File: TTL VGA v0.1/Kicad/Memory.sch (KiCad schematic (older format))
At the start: 14 parts, among them U10 UM61512A, U11 74LS245, U12 74LS374, U13 74LS245, U14 74LS245, U6 G22V10, U7 G22V10, U8 74LS139, U9 UM61512A

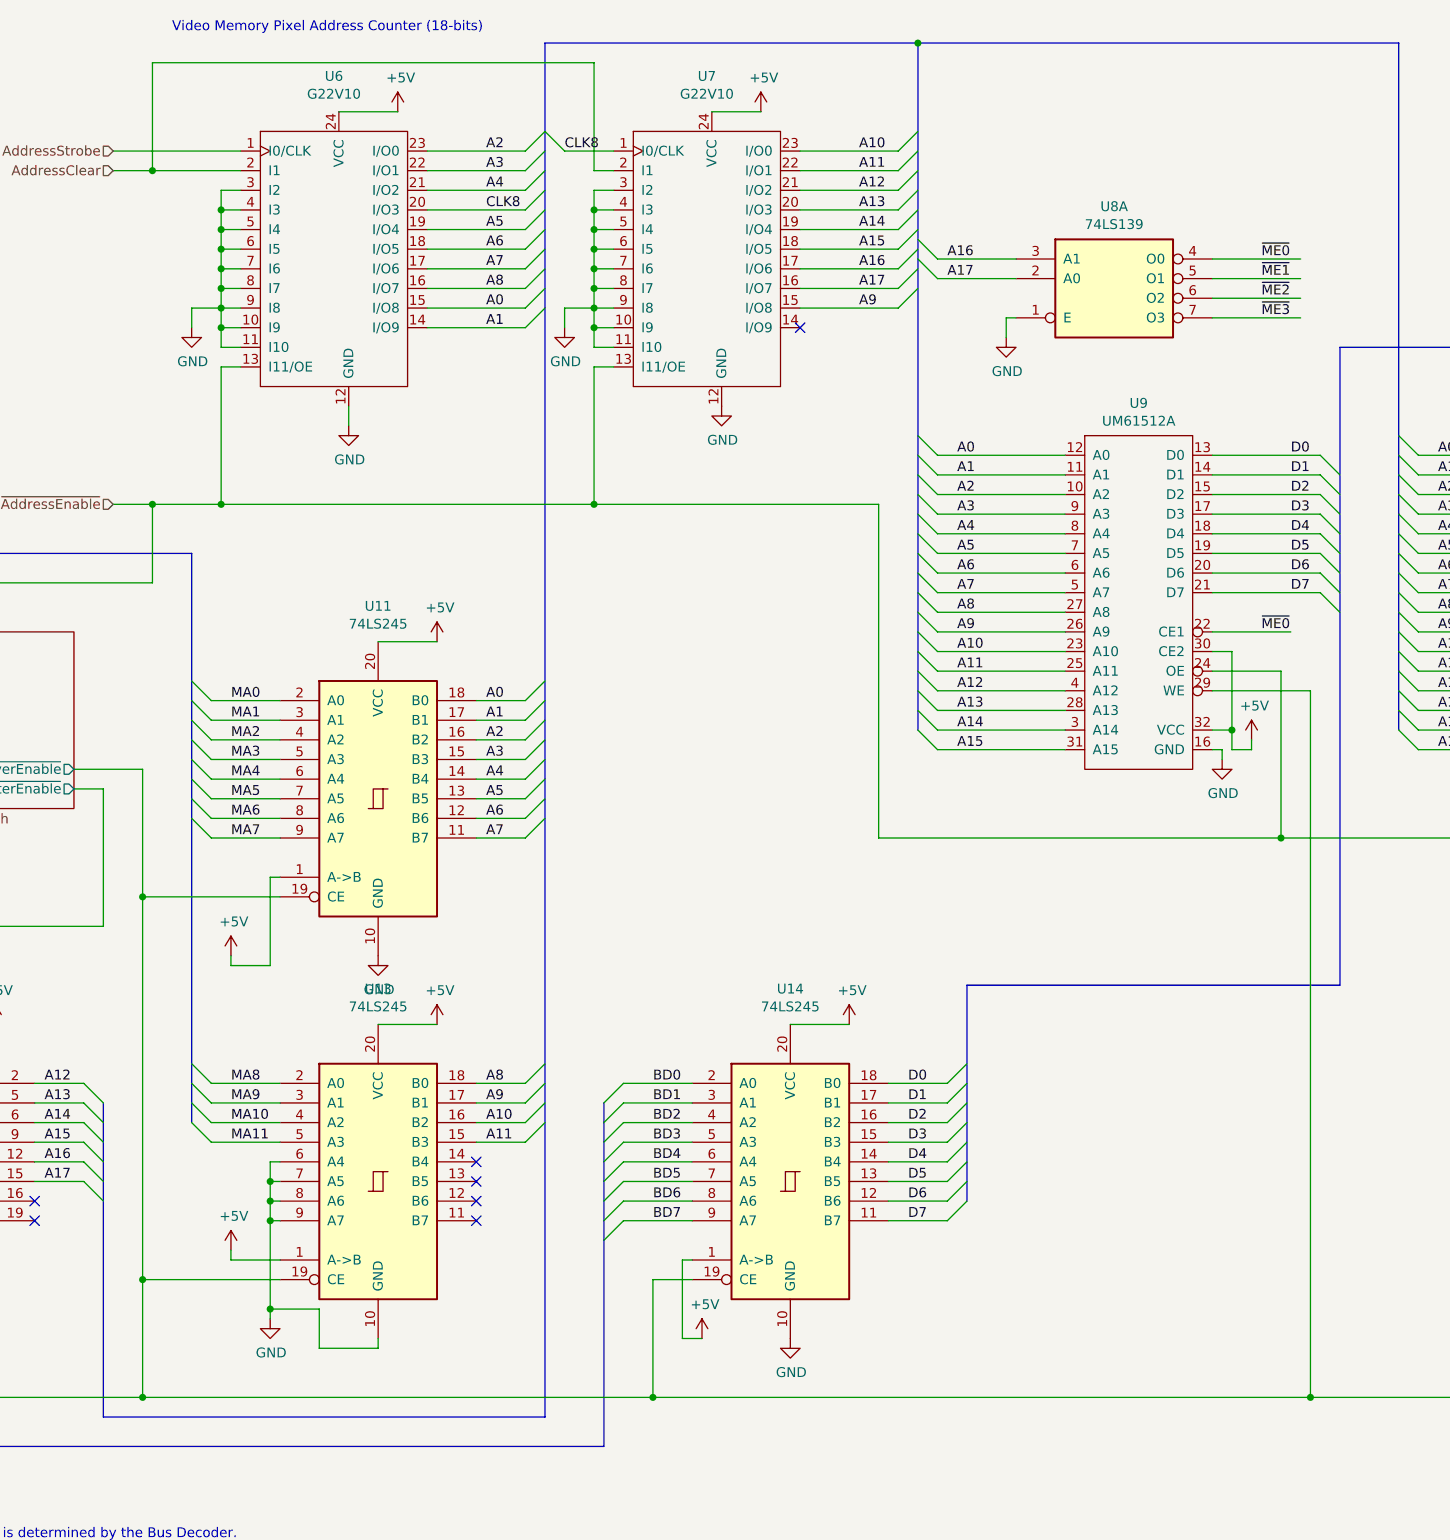
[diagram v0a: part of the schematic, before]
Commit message: vga memory interface
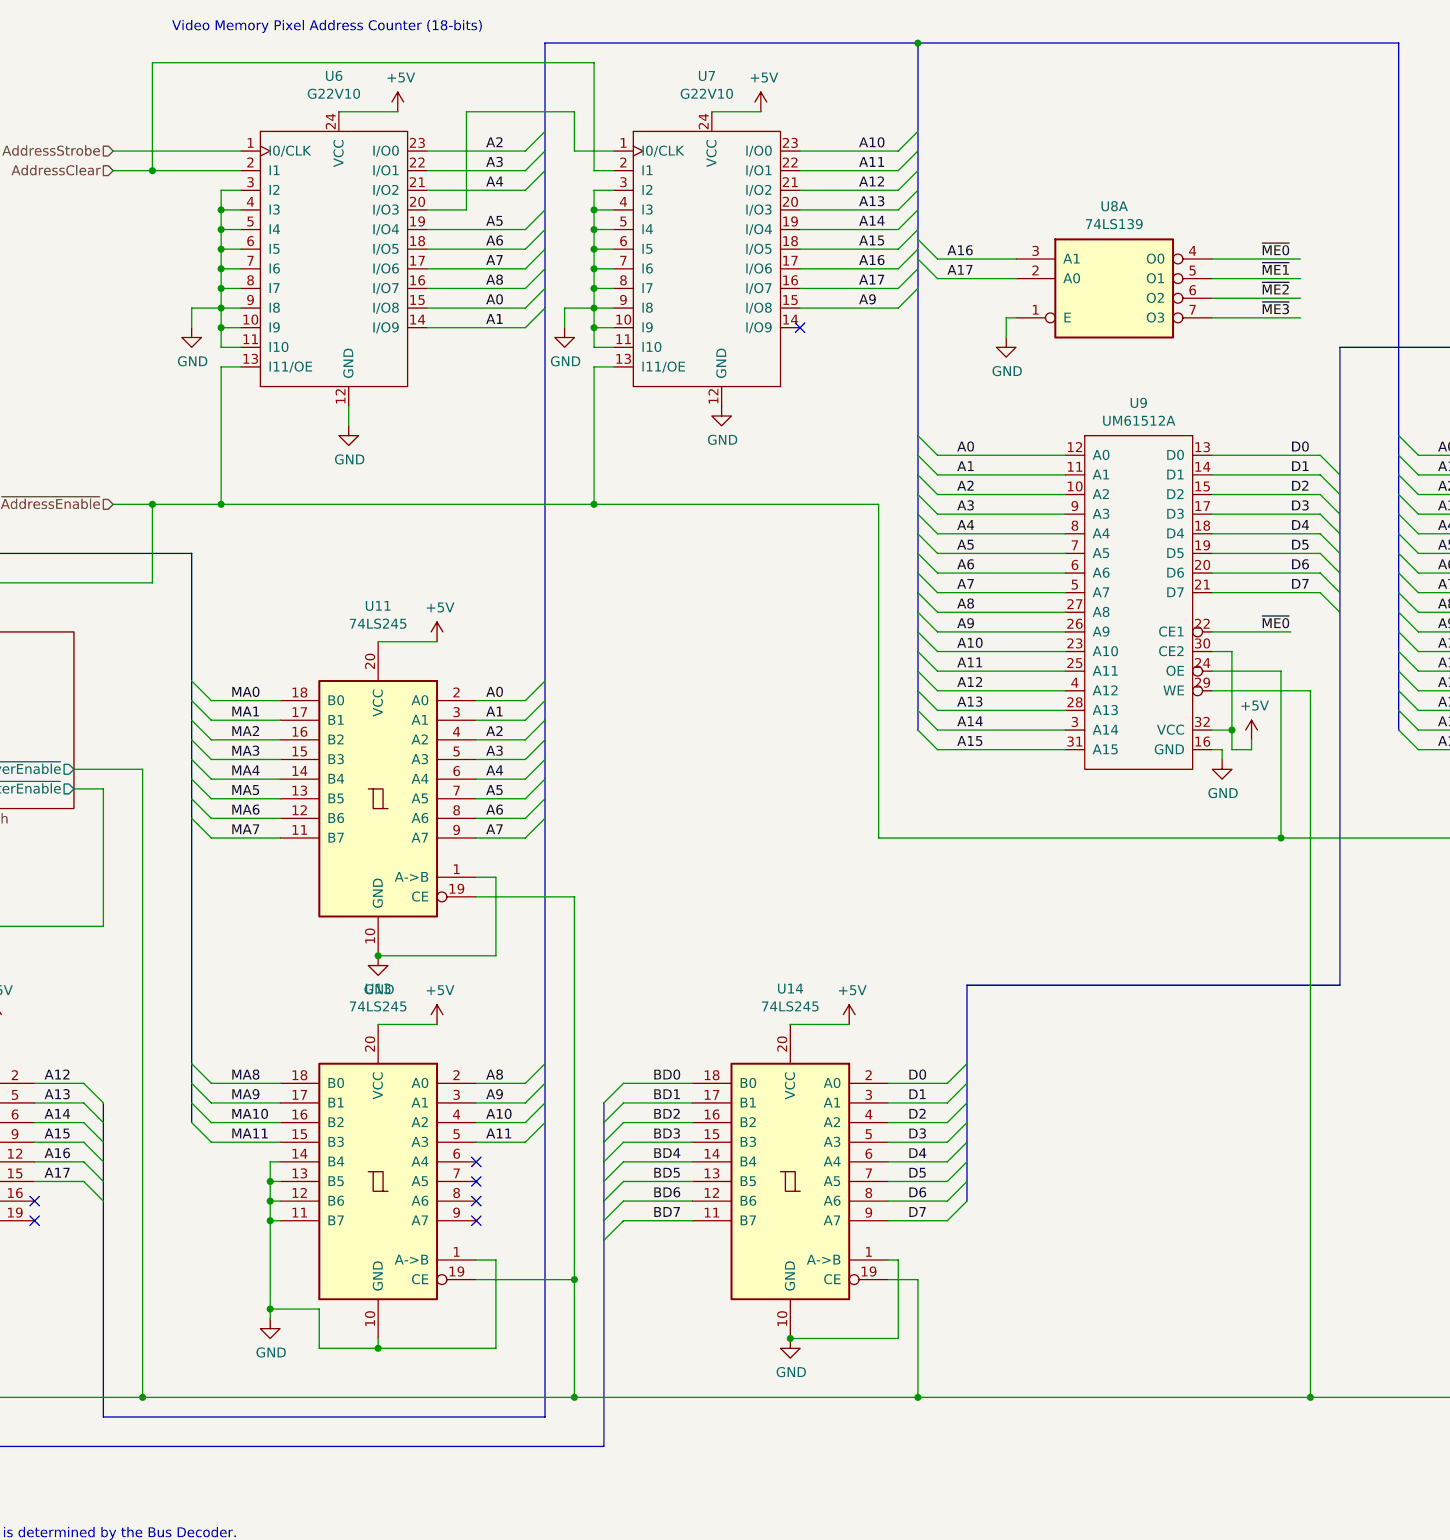
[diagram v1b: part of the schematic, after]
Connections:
- net +5V: no longer U11.1 (A->B), U13.1 (A->B), U14.1 (A->B)
- net A0: now also U11.2 (A0); no longer U11.18 (B0)
- net A1: now also U11.3 (A1); no longer U11.17 (B1)
- net A10: now also U13.4 (A2); no longer U13.16 (B2)
- net A11: now also U13.5 (A3); no longer U13.15 (B3)
- net A2: now also U11.4 (A2); no longer U11.16 (B2)
- net A3: now also U11.5 (A3); no longer U11.15 (B3)
- net A4: now also U11.6 (A4); no longer U11.14 (B4)
- net A5: now also U11.7 (A5); no longer U11.13 (B5)
- net A6: now also U11.8 (A6); no longer U11.12 (B6)
- net A7: now also U11.9 (A7); no longer U11.11 (B7)
- net A8: now also U13.2 (A0); no longer U13.18 (B0)
- net A9: now also U13.3 (A1); no longer U13.17 (B1)
- net BD0: now also U14.18 (B0); no longer U14.2 (A0)
- net BD1: now also U14.17 (B1); no longer U14.3 (A1)
- net BD2: now also U14.16 (B2); no longer U14.4 (A2)
- net BD3: now also U14.15 (B3); no longer U14.5 (A3)
- net BD4: now also U14.14 (B4); no longer U14.6 (A4)
- net BD5: now also U14.13 (B5); no longer U14.7 (A5)
- net BD6: now also U14.12 (B6); no longer U14.8 (A6)
- net BD7: now also U14.11 (B7); no longer U14.9 (A7)
- net D0: now also U14.2 (A0); no longer U14.18 (B0)
- net D1: now also U14.3 (A1); no longer U14.17 (B1)
- net D2: now also U14.4 (A2); no longer U14.16 (B2)
- net D3: now also U14.5 (A3); no longer U14.15 (B3)
- net D4: now also U14.6 (A4); no longer U14.14 (B4)
- net D5: now also U14.7 (A5); no longer U14.13 (B5)
- net D6: now also U14.8 (A6); no longer U14.12 (B6)
- net D7: now also U14.9 (A7); no longer U14.11 (B7)
- net GND: now also U11.1 (A->B), U13.1 (A->B), U13.11 (B7), U13.12 (B6), U13.13 (B5), U13.14 (B4), U14.1 (A->B); no longer U13.6 (A4), U13.7 (A5), U13.8 (A6), U13.9 (A7)
- net MA0: now also U11.18 (B0); no longer U11.2 (A0)
- net MA1: now also U11.17 (B1); no longer U11.3 (A1)
- net MA10: now also U13.16 (B2); no longer U13.4 (A2)
- net MA11: now also U13.15 (B3); no longer U13.5 (A3)
- net MA2: now also U11.16 (B2); no longer U11.4 (A2)
- net MA3: now also U11.15 (B3); no longer U11.5 (A3)
- net MA4: now also U11.14 (B4); no longer U11.6 (A4)
- net MA5: now also U11.13 (B5); no longer U11.7 (A5)
- net MA6: now also U11.12 (B6); no longer U11.8 (A6)
- net MA7: now also U11.11 (B7); no longer U11.9 (A7)
- net MA8: now also U13.18 (B0); no longer U13.2 (A0)
- net MA9: now also U13.17 (B1); no longer U13.3 (A1)
- net CLK8: no longer names the net of U6.20 (I/O3), U7.1 (I0/CLK)
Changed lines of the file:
@@
-$Comp
-L 74xx:74LS139 U8
-U 1 1 5E4CEB46
-P 8100 2300
-F 0 "U8" H 8100 2667 50  0000 C CNN
-F 1 "74LS139" H 8100 2576 50  0000 C CNN
-F 2 "" H 8100 2300 50  0001 C CNN
-F 3 "http://www.ti.com/lit/gpn/sn74LS139" H 8100 2300 50  0001 C CNN
-	1    8100 2300
-	1    0    0    -1
-$EndComp
 $Comp
 L 74xx:74LS139 U8
@@
 	4600 1850 5100 1850
 Wire Wire Line
-	4600 1950 5100 1950
-Wire Wire Line
 	4600 2050 5100 2050
 Wire Wire Line
@@
 Text Label 4900 1850 0    50   ~ 0
 A4
-Text Label 4900 1950 0    50   ~ 0
-CLK8
 Text Label 4900 2050 0    50   ~ 0
 A5
@@
 Entry Wire Line
 	5100 1850 5200 1750
-Entry Wire Line
-	5100 1950 5200 1850
 Entry Wire Line
 	5100 2050 5200 1950
@@
 F 3 "http://www.ti.com/lit/gpn/sn74LS245" H 4350 4950 50  0001 C CNN
 	1    4350 4950
-	1    0    0    -1
+	-1   0    0    -1
 $EndComp
 Entry Wire Line
@@
 F 3 "http://www.ti.com/lit/gpn/sn74LS245" H 4350 6900 50  0001 C CNN
 	1    4350 6900
-	1    0    0    -1
+	-1   0    0    -1
 $EndComp
 Wire Wire Line
@@
 F6 "~AddressEnable" I L 1750 4250 50
 $EndSheet
-Wire Wire Line
-	3150 4800 3150 5450
-Wire Wire Line
-	3150 7400 3850 7400
-Wire Wire Line
-	3850 5450 3150 5450
-Connection ~ 3150 5450
-Wire Wire Line
-	3150 5450 3150 7400
 Entry Wire Line
 	1250 6300 1350 6400
@@
 Wire Wire Line
 	1600 7400 1350 7400
-Connection ~ 3150 7400
 Entry Wire Line
 	2850 6400 2950 6500
@@
 NoConn ~ 4850 6800
 NoConn ~ 4850 6900
-NoConn ~ 4850 7000
-NoConn ~ 4850 7100
 Wire Wire Line
 	1100 5600 1100 7300
@@
 Wire Wire Line
 	1350 7400 1350 8000
-Wire Wire Line
-	3150 7400 3150 8000
 $Comp
 L power:+5V #PWR023
@@
 Z80 interfaces through a 4k Memory Page. \nThe location (bit address) of this memory page is determined by the Bus Decoder.\n\nThe Control Register provides the upper 6 bits A12..A17 of the\nVRAM address and can only be changed through an IO write.\nThe IO address (A0-A7) is also determined by the Bus Decoder.
 Wire Wire Line
-	3850 5350 3800 5350
-Wire Wire Line
 	3800 6800 3800 6900
 Wire Wire Line
@@
 F 3 "http://www.ti.com/lit/gpn/sn74LS245" H 6450 6900 50  0001 C CNN
 	1    6450 6900
-	1    0    0    -1
+	-1   0    0    -1
 $EndComp
 Wire Wire Line
@@
 BD7
 Wire Wire Line
-	3150 8000 5750 8000
-Wire Wire Line
-	5750 8000 5750 7400
-Wire Wire Line
-	5750 7400 5950 7400
+	3150 8000 5350 8000
 Connection ~ 3150 8000
-Wire Wire Line
-	5950 7300 5900 7300
 $Comp
 L power:GND #PWR031
@@
 Wire Bus Line
 	5500 8250 1250 8250
-$Comp
-L power:+5V #PWR021
-U 1 1 5E4D5D75
-P 3600 5750
-F 0 "#PWR021" H 3600 5600 50  0001 C CNN
-F 1 "+5V" H 3615 5923 50  0000 C CNN
-F 2 "" H 3600 5750 50  0001 C CNN
-F 3 "" H 3600 5750 50  0001 C CNN
-	1    3600 5750
-	1    0    0    -1
-$EndComp
-$Comp
-L power:+5V #PWR026
-U 1 1 5E4D64EC
-P 3600 7250
-F 0 "#PWR026" H 3600 7100 50  0001 C CNN
-F 1 "+5V" H 3615 7423 50  0000 C CNN
-F 2 "" H 3600 7250 50  0001 C CNN
-F 3 "" H 3600 7250 50  0001 C CNN
-	1    3600 7250
-	1    0    0    -1
-$EndComp
-$Comp
-L power:+5V #PWR030
-U 1 1 5E4D69CD
-P 6000 7700
-F 0 "#PWR030" H 6000 7550 50  0001 C CNN
-F 1 "+5V" H 6015 7873 50  0000 C CNN
-F 2 "" H 6000 7700 50  0001 C CNN
-F 3 "" H 6000 7700 50  0001 C CNN
-	1    6000 7700
-	1    0    0    -1
-$EndComp
-Wire Wire Line
-	5900 7300 5900 7700
-Wire Wire Line
-	5900 7700 6000 7700
-Wire Wire Line
-	3850 7300 3600 7300
-Wire Wire Line
-	3600 7300 3600 7250
-Wire Wire Line
-	3800 5350 3800 5800
-Wire Wire Line
-	3800 5800 3600 5800
-Wire Wire Line
-	3600 5800 3600 5750
 Entry Wire Line
 	7250 6400 7350 6300
@@
 	8600 4400 9100 4400
 Wire Wire Line
-	9100 8000 5750 8000
-Connection ~ 5750 8000
+	9100 8000 7100 8000
 Wire Wire Line
 	6900 3450 6900 5150
@@
 	1    0    0    -1
 $EndComp
-Entry Wire Line
-	5200 1550 5300 1650
-Wire Wire Line
-	5300 1650 5550 1650
-Text Label 5300 1650 0    50   ~ 0
-CLK8
 Wire Wire Line
 	6050 1450 6300 1450
@@
 Wire Wire Line
 	7000 2450 6500 2450
-Wire Bus Line
-	2950 6500 2950 8100
-Wire Bus Line
-	11700 2650 11700 4000
-Wire Bus Line
-	7350 5900 7350 7000
-Wire Bus Line
-	5500 6500 5500 8250
-Wire Bus Line
-	1250 4950 1250 8250
-Wire Bus Line
-	9250 2650 9250 5900
-Wire Bus Line
-	3400 3700 3400 6600
-Wire Bus Line
-	9550 1100 9550 4600
-Wire Bus Line
-	5200 1100 5200 8100
-Wire Bus Line
-	7100 1100 7100 4600
 Text Label 6800 2050 0    50   ~ 0
 A14
@@
 Text Label 6800 2450 0    50   ~ 0
 A9
+$Comp
+L 74xx:74LS139 U8
+U 1 1 5E4CEB46
+P 8100 2300
+F 0 "U8" H 8100 2667 50  0000 C CNN
+F 1 "74LS139" H 8100 2576 50  0000 C CNN
+F 2 "" H 8100 2300 50  0001 C CNN
+F 3 "http://www.ti.com/lit/gpn/sn74LS139" H 8100 2300 50  0001 C CNN
+	1    8100 2300
+	1    0    0    -1
+$EndComp
+Wire Wire Line
+	4600 1950 4800 1950
+Wire Wire Line
+	4800 1950 4800 1450
+Wire Wire Line
+	4800 1450 5350 1450
+Wire Wire Line
+	5350 1450 5350 1650
+Wire Wire Line
+	5350 1650 5550 1650
+Wire Wire Line
+	4850 5350 4950 5350
+Wire Wire Line
+	4950 5350 4950 5750
+Wire Wire Line
+	4950 5750 4350 5750
+Connection ~ 4350 5750
+Wire Wire Line
+	4850 7300 4950 7300
+Wire Wire Line
+	4950 7300 4950 7750
+Wire Wire Line
+	4950 7750 4350 7750
+Connection ~ 4350 7750
+Wire Wire Line
+	5350 8000 5350 7400
+Wire Wire Line
+	5350 5450 4850 5450
+Connection ~ 5350 8000
+Wire Wire Line
+	4850 7400 5350 7400
+Connection ~ 5350 7400
+Wire Wire Line
+	5350 7400 5350 5450
+Wire Wire Line
+	3150 4800 3150 8000
+Wire Wire Line
+	6950 7300 7000 7300
+Wire Wire Line
+	7000 7300 7000 7700
+Wire Wire Line
+	7000 7700 6450 7700
+Connection ~ 6450 7700
+Wire Wire Line
+	6950 7400 7100 7400
+Wire Wire Line
+	7100 7400 7100 8000
+Connection ~ 7100 8000
+Wire Wire Line
+	5350 8000 7100 8000
+NoConn ~ 4850 7000
+NoConn ~ 4850 7100
+Wire Bus Line
+	2950 6500 2950 8100
+Wire Bus Line
+	11700 2650 11700 4000
+Wire Bus Line
+	7350 5900 7350 7000
+Wire Bus Line
+	5500 6500 5500 8250
+Wire Bus Line
+	1250 4950 1250 8250
+Wire Bus Line
+	9250 2650 9250 5900
+Wire Bus Line
+	3400 3700 3400 6600
+Wire Bus Line
+	9550 1100 9550 4600
+Wire Bus Line
+	5200 1100 5200 8100
+Wire Bus Line
+	7100 1100 7100 4600
 $EndSCHEMATC

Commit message: vga work
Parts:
- added JP?: Jumper, symbol Device:Jumper
- added R?: 10k, symbol Device:R
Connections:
- net +5V: now also R?.1
- net ~AddressEnable: now also JP?.1; no longer U10.24 (OE), U6.13 (I11/OE), U7.13 (I11/OE), U9.24 (OE)
- new net Bus Decoder/~AddressEnable: JP?.2, R?.2, U10.24 (OE), U6.13 (I11/OE), U7.13 (I11/OE), U9.24 (OE)
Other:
- note added: "This jumper is to disable the VGA VRAM access (removed).\nThis allows the SystemController to easily perform tests \nand access VRAM without synchronization.\n"
- note added: "We could have registers here that load in a start address for \neach frame. That way a scrolling function can be supported \nin hardware. The software would load a value of the address \nof the start of the next frame based on the direction of scrolling. \nLeft or right would simply increment or decrement the start \naddress. Scrolling up and down would be addding/subtracting \na complete horizon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"
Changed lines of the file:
@@
 Entry Wire Line
 	5100 5150 5200 5050
-Text HLabel 3000 3450 0    50   Input ~ 0
+Text HLabel 1250 3050 0    50   Input ~ 0
 ~AddressEnable
 Wire Wire Line
@@
 $EndComp
 NoConn ~ 2600 7000
-NoConn ~ 2600 7100
 $Comp
 L 74xx:74LS245 U14
@@
 	1750 4550 1100 4550
 Wire Wire Line
-	1600 3850 1600 4250
-Wire Wire Line
-	1600 4250 1750 4250
-Wire Wire Line
 	4600 2550 5100 2550
 $Comp
@@
 Wire Bus Line
 	7100 1100 9550 1100
-Wire Wire Line
-	3000 3450 3200 3450
-Wire Wire Line
-	3200 3450 3200 3850
-Connection ~ 3200 3450
-Wire Wire Line
-	3200 3450 3550 3450
-Wire Wire Line
-	3200 3850 1600 3850
 Wire Wire Line
 	4450 1450 4150 1450
@@
 NoConn ~ 4850 7000
 NoConn ~ 4850 7100
+Text Notes 550  1450 0    50   ~ 0
+We could have registers here that load in a start address for \neach frame. That way a scrolling function can be supported \nin hardware. The software would load a value of the address \nof the start of the next frame based on the direction of scrolling. \nLeft or right would simply increment or decrement the start \naddress. Scrolling up and down would be addding/subtracting \na complete horizontal line worth of bytes.
+Text Notes 750  2650 0    50   ~ 0
+This jumper is to disable the VGA VRAM access (removed).\nThis allows the SystemController to easily perform tests \nand access VRAM without synchronization.\n
+Wire Wire Line
+	1600 3050 1250 3050
+$Comp
+L Device:Jumper JP?
+U 1 1 5EBC403C
+P 1900 3050
+F 0 "JP?" H 1900 3314 50  0000 C CNN
+F 1 "Jumper" H 1900 3223 50  0000 C CNN
+F 2 "" H 1900 3050 50  0001 C CNN
+F 3 "~" H 1900 3050 50  0001 C CNN
+	1    1900 3050
+	1    0    0    -1
+$EndComp
+Wire Wire Line
+	2200 3050 2450 3050
+Wire Wire Line
+	2450 3050 2450 3450
+Wire Wire Line
+	2450 3450 2950 3450
+Wire Wire Line
+	1500 4250 1500 3450
+Wire Wire Line
+	1500 3450 2450 3450
+Wire Wire Line
+	1500 4250 1750 4250
+Connection ~ 2450 3450
+$Comp
+L Device:R R?
+U 1 1 5EC03DFE
+P 2950 3150
+F 0 "R?" H 3020 3196 50  0000 L CNN
+F 1 "10k" H 3020 3105 50  0000 L CNN
+F 2 "" V 2880 3150 50  0001 C CNN
+F 3 "~" H 2950 3150 50  0001 C CNN
+	1    2950 3150
+	1    0    0    -1
+$EndComp
+Wire Wire Line
+	2950 3300 2950 3450
+Connection ~ 2950 3450
+Wire Wire Line
+	2950 3450 3550 3450
+Wire Wire Line
+	2950 3000 2950 2900
+$Comp
+L power:+5V #PWR?
+U 1 1 5EC43E14
+P 2950 2900
+F 0 "#PWR?" H 2950 2750 50  0001 C CNN
+F 1 "+5V" H 2965 3073 50  0000 C CNN
+F 2 "" H 2950 2900 50  0001 C CNN
+F 3 "" H 2950 2900 50  0001 C CNN
+	1    2950 2900
+	1    0    0    -1
+$EndComp
+NoConn ~ 2600 7100
 Wire Bus Line
 	2950 6500 2950 8100

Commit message: More VGA work
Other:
- note added: "A16 and A17 are swapped on the 74LS139.\n(but it is wired like this on the perf board)\nThis will fail when using more VRAM chips.\nFix by swapping outputs in U7 (WinCUPL)."
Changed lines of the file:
@@
 Wire Bus Line
 	7100 1100 7100 4600
+Text Notes 7250 1800 0    50   ~ 0
+A16 and A17 are swapped on the 74LS139.\n(but it is wired like this on the perf board)\nThis will fail when using more VRAM chips.\nFix by swapping outputs in U7 (WinCUPL).
 $EndSCHEMATC
